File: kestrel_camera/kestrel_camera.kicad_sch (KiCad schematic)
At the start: 0 parts

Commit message: sensor pcb setup
creates kicad project for AISC110C sensor breakout board
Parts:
- added U1: (no value), AISC110C:AISC110C, symbol aisc110c:AISC110C
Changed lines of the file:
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@@
 	(generator_version "10.0")
 	(paper "A4")
+	(symbol
+		(lib_id "aisc110c:AISC110C")
+		(at 68.58 80.01 0)
+		(unit 1)
+		(body_style 1)
+		(exclude_from_sim no)
+		(in_bom yes)
+		(on_board yes)
+		(in_pos_files yes)
+		(dnp no)
+		(fields_autoplaced yes)
+		(property "Reference" "U1"
+			(at 83.4233 133.35 0)
+			(show_name no)
+			(do_not_autoplace no)
+			(effects
+				(font
+					(size 1.27 1.27)
+				)
+				(justify left)
+			)
+		)
+		(property "Value" ""
+			(at 68.58 80.01 0)
+			(show_name no)
+			(do_not_autoplace no)
+			(effects
+				(font
+					(size 1.27 1.27)
+				)
+			)
+		)
+		(property "Footprint" "AISC110C:AISC110C"
+			(at 68.58 80.01 0)
+			(hide yes)
+			(show_name no)
+			(do_not_autoplace no)
+			(effects
+				(font
+					(size 1.27 1.27)
+				)
+			)
+		)
+		(property "Datasheet" ""
+			(at 68.58 80.01 0)
+			(hide yes)
+			(show_name no)
+			(do_not_autoplace no)
+			(effects
+				(font
+					(size 1.27 1.27)
+				)
+			)
+		)
+		(property "Description" ""
+			(at 68.58 80.01 0)
+			(hide yes)
+			(show_name no)
+			(do_not_autoplace no)
+			(effects
+				(font
+					(size 1.27 1.27)
+				)
+			)
+		)
+		(pin "22"
+		)
+		(pin "9"
+		)
+		(pin "14"
+		)
+		(pin "26"
+		)
+		(pin "1"
+		)
+		(pin "28"
+		)
+		(pin "13"
+		)
+		(pin "18"
+		)
+		(pin "15"
+		)
+		(pin "21"
+		)
+		(pin "6"
+		)
+		(pin "17"
+		)
+		(pin "3"
+		)
+		(pin "4"
+		)
+		(pin "8"
+		)
+		(pin "20"
+		)
+		(pin "19"
+		)
+		(pin "12"
+		)
+		(pin "16"
+		)
+		(pin "10"
+		)
+		(pin "7"
+		)
+		(pin "11"
+		)
+		(pin "2"
+		)
+		(pin "5"
+		)
+		(pin "23"
+		)
+		(pin "24"
+		)
+		(pin "25"
+		)
+		(pin "27"
+		)
+		(pin "34"
+		)
+		(pin "47"
+		)
+		(pin "35"
+		)
+		(pin "51"
+		)
+		(pin "53"
+		)
+		(pin "55"
+		)
+		(pin "45"
+		)
+		(pin "49"
+		)
+		(pin "32"
+		)
+		(pin "46"
+		)
+		(pin "62"
+		)
+		(pin "40"
+		)
+		(pin "44"
+		)
+		(pin "39"
+		)
+		(pin "59"
+		)
+		(pin "36"
+		)
+		(pin "31"
+		)
+		(pin "29"
+		)
+		(pin "33"
+		)
+		(pin "38"
+		)
+		(pin "37"
+		)
+		(pin "42"
+		)
+		(pin "43"
+		)
+		(pin "30"
+		)
+		(pin "41"
+		)
+		(pin "48"
+		)
+		(pin "50"
+		)
+		(pin "52"
+		)
+		(pin "54"
+		)
+		(pin "56"
+		)
+		(pin "57"
+		)
+		(pin "58"
+		)
+		(pin "60"
+		)
+		(pin "61"
+		)
+		(pin "63"
+		)
+		(pin "64"
+		)
+		(instances
+			(project "kestrel_camera"
+				(path "/97a847c9-d989-41dc-b959-cfc0f8d7a8bf"
+					(reference "U1")
+					(unit 1)
+				)
+			)
+		)
+	)
 	(sheet_instances
 		(path "/"

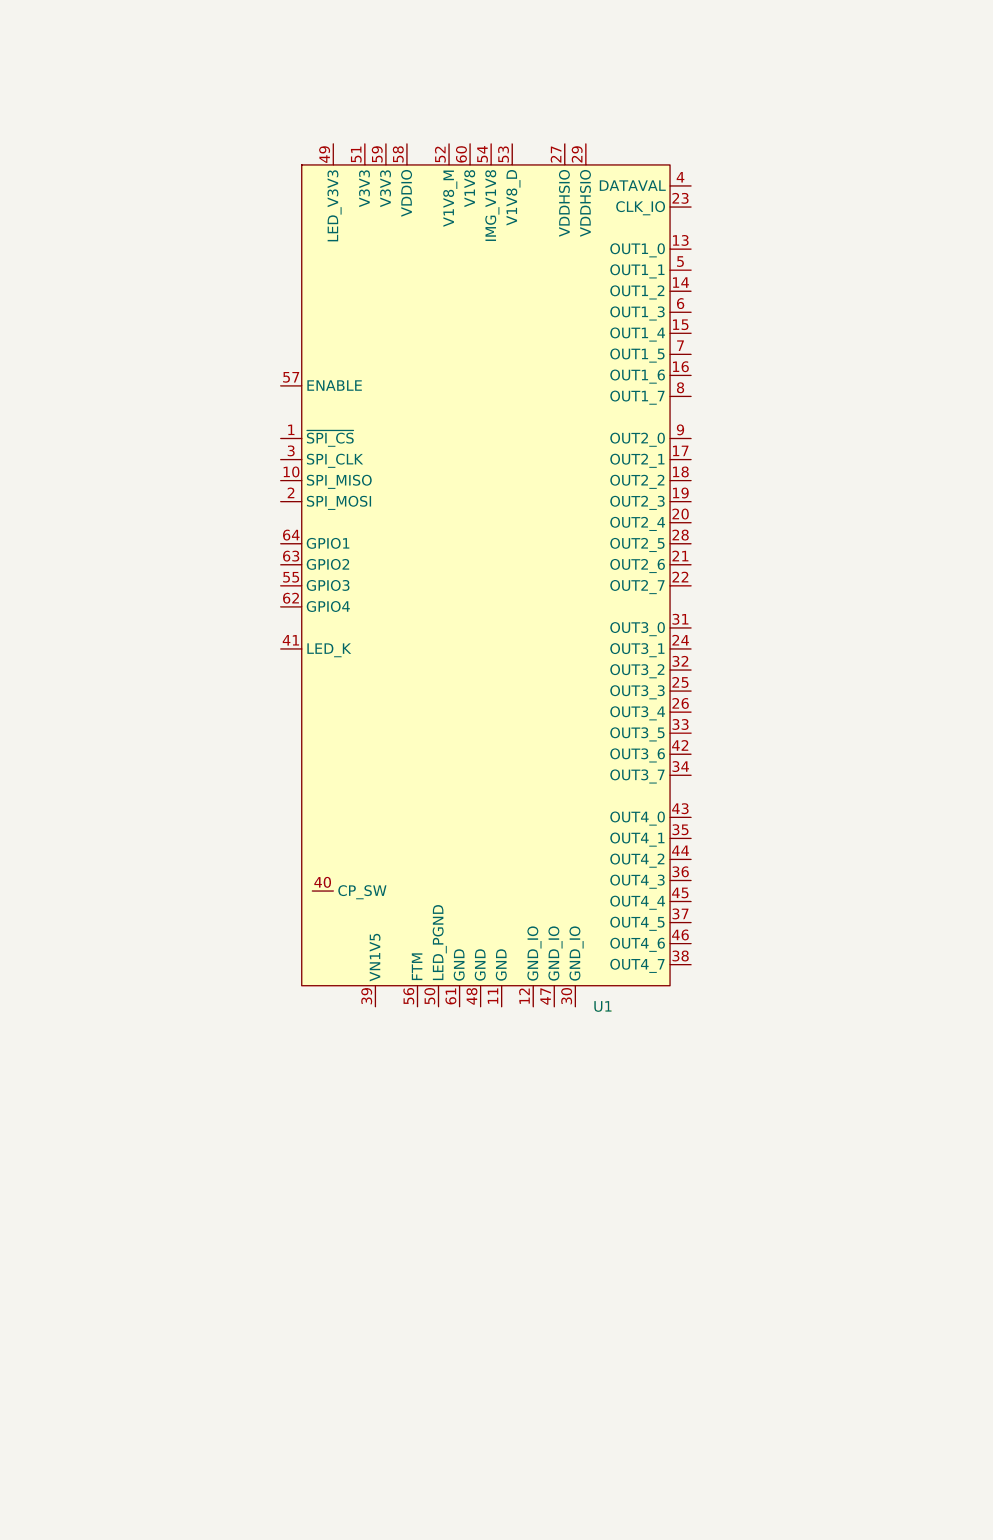
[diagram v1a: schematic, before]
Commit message: beginning setup for aisc110c sensor ic
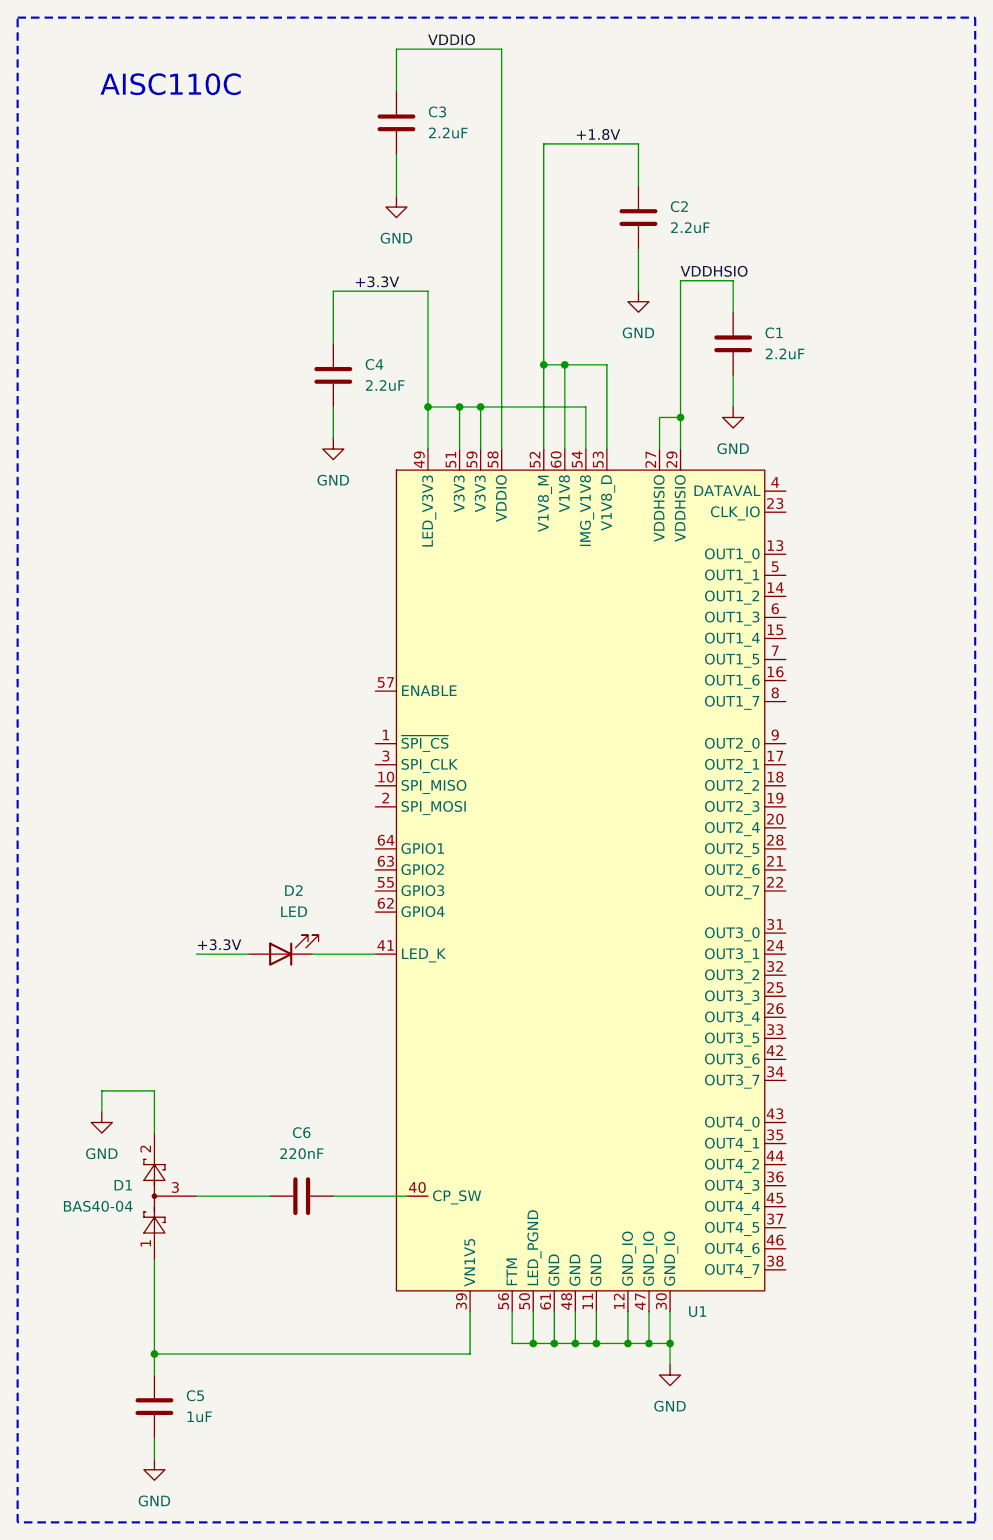
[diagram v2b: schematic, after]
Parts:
- added C1, C2, C3, C4: 2.2uF, symbol Device:C
- added C5: 1uF, symbol Device:C
- added C6: 220nF, symbol Device:C
- added D1: BAS40-04, Package_TO_SOT_SMD:SOT-23, symbol Diode:BAS40-04
- added D2: LED, symbol Device:LED
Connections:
- net GND: now reaches U1.11 (GND)
- net GND: now also U1.12 (GND_IO), U1.30 (GND_IO), U1.47 (GND_IO), U1.48 (GND), U1.50 (LED_PGND), U1.56 (FTM), U1.61 (GND), C1.2, C2.2, C3.2, C4.2, C5.2, D1.2
- net VDDHSIO: now reaches U1.27 (VDDHSIO)
- net VDDHSIO: now also U1.29 (VDDHSIO), C1.1
- net at U1.39 (VN1V5): now also C5.1, D1.1
- net at U1.40 (CP_SW): now also C6.2
- net at U1.41 (LED_K): now also D2.1 (K)
- net +3.3V: now reaches U1.49 (LED_V3V3)
- net +3.3V: now also U1.51 (V3V3), U1.54 (IMG_V1V8), U1.59 (V3V3), C4.1, D2.2 (A)
- net +1.8V: now reaches U1.52 (V1V8_M)
- net +1.8V: now also U1.53 (V1V8_D), U1.60 (V1V8), C2.1
- net VDDIO: now reaches U1.58 (VDDIO)
- net VDDIO: now also C3.1
- new net: C6.1, D1.3
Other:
- note added: "AISC110C"
- moved on the sheet: U1

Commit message: aisc110c fmc-hpc board schematic - revision 1
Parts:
- removed D1: BAS40-04, Package_TO_SOT_SMD:SOT-23, symbol Diode:BAS40-04
- added CR1: BAS40-04-E3-08, BAS40_04_E3_08:SOT_04-HE3-08_VIS, symbol BAS40_04_E3_08:BAS40-04-E3-08
- added J1: ASP-134602-01, ASP-134602-01:SAMTEC_ASP-134602-01, symbol ASP-134602-01:ASP-134602-01
- added J2: DEBUG_HEADER, Connector_PinHeader_2.54mm:PinHeader_2x08_P2.54mm_Vertical, symbol Connector_Generic_MountingPin:Conn_02x08_Odd_Even_MountingPin
- added R1: 10kR, Resistor_SMD:R_0603_1608Metric, symbol Device:R
- added TP1: V1V8_PWR, TestPoint:TestPoint_Pad_3.0x3.0mm, symbol Connector:TestPoint
- added TP10: D4_0, TestPoint:TestPoint_Pad_D1.5mm, symbol Connector:TestPoint
- added TP2: VDD_HSIO, TestPoint:TestPoint_Pad_3.0x3.0mm, symbol Connector:TestPoint
- added TP3: V3V3_PWR, TestPoint:TestPoint_Pad_3.0x3.0mm, symbol Connector:TestPoint
- added TP4: VN1V5_PWR, TestPoint:TestPoint_Pad_3.0x3.0mm, symbol Connector:TestPoint
- added TP5: CLK_IO, TestPoint:TestPoint_Pad_D1.5mm, symbol Connector:TestPoint
- added TP6: DATAVALID, TestPoint:TestPoint_Pad_D1.5mm, symbol Connector:TestPoint
- added TP7: D1_0, TestPoint:TestPoint_Pad_D1.5mm, symbol Connector:TestPoint
- added TP8: D2_0, TestPoint:TestPoint_Pad_D1.5mm, symbol Connector:TestPoint
- added TP9: D3_0, TestPoint:TestPoint_Pad_D1.5mm, symbol Connector:TestPoint
- C1, C2, C3, C4, C5, C6: footprint (none) -> Capacitor_SMD:C_0603_1608Metric
- D1: renamed from D2; footprint (none) -> LED_SMD:LED_0603_1608Metric
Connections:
- net VDDIO is gone; now on net V1V8: C3.1, U1.58 (VDDIO)
- net GND: now also CR1.1, J1.A1, J1.A12, J1.A13, J1.A16, J1.A17, J1.A20, J1.A21, J1.A24, J1.A25, J1.A28, J1.A29, J1.A32, J1.A33, J1.A36, J1.A37, J1.A4, J1.A40, J1.A5, J1.A8, J1.A9, J1.B10, J1.B11, J1.B14, J1.B15, J1.B18, J1.B19, J1.B2, J1.B22, J1.B23, J1.B26, J1.B27, J1.B3, J1.B30, J1.B31, J1.B34, J1.B35, J1.B38, J1.B39, J1.B6, J1.B7, J1.C1, J1.C12, J1.C13, J1.C16, J1.C17, J1.C20, J1.C21, J1.C24, J1.C25, J1.C28, J1.C29, J1.C32, J1.C33, J1.C36, J1.C38, J1.C4, J1.C40, J1.C5, J1.C8, J1.C9, J1.D10, J1.D13, J1.D16, J1.D19, J1.D2, J1.D22, J1.D25, J1.D28, J1.D3, J1.D37, J1.D39, J1.D6, J1.D7, J1.E1, J1.E11, J1.E14, J1.E17, J1.E20, J1.E23, J1.E26, J1.E29, J1.E32, J1.E35, J1.E38, J1.E4, J1.E40, J1.E5, J1.E8, J1.F12, J1.F15, J1.F18, J1.F2, J1.F21, J1.F24, J1.F27, J1.F3, J1.F30, J1.F33, J1.F36, J1.F39, J1.F6, J1.F9, J1.G1, J1.G11, J1.G14, J1.G17, J1.G20, J1.G23, J1.G26, J1.G29, J1.G32, J1.G35, J1.G38, J1.G4, J1.G40, J1.G5, J1.G8, J1.H12, J1.H15, J1.H18, J1.H21, J1.H24, J1.H27, J1.H3, J1.H30, J1.H33, J1.H36, J1.H39, J1.H6, J1.H9, J1.J1, J1.J11, J1.J14, J1.J17, J1.J20, J1.J23, J1.J26, J1.J29, J1.J32, J1.J35, J1.J38, J1.J4, J1.J40, J1.J5, J1.J8, J1.K12, J1.K15, J1.K18, J1.K2, J1.K21, J1.K24, J1.K27, J1.K3, J1.K30, J1.K33, J1.K36, J1.K39, J1.K40, J1.K6, J1.K9, J2.1 (Pin_1), J2.10 (Pin_10), J2.11 (Pin_11), J2.2 (Pin_2), J2.6 (Pin_6), J2.MP (MountPin), R1.2
- net VDDHSIO: now also TP2.1
- net SPI_CS: now reaches U1.1 (~{SPI_CS})
- net SPI_CS: now also J1.D8, J2.3 (Pin_3)
- net SPI_MISO: now reaches U1.10 (SPI_MISO)
- net SPI_MISO: now also J1.J24, J2.7 (Pin_7)
- net D1_0: now reaches U1.13 (OUT1_0)
- net D1_0: now also J1.C10, TP7.1
- net D1_2: now reaches U1.14 (OUT1_2)
- net D1_2: now also J1.D11
- net D1_4: now reaches U1.15 (OUT1_4)
- net D1_4: now also J1.H8
- net D1_6: now reaches U1.16 (OUT1_6)
- net D1_6: now also J1.H13
- net D2_1: now reaches U1.17 (OUT2_1)
- net D2_1: now also J1.H20
- net D2_2: now reaches U1.18 (OUT2_2)
- net D2_2: now also J1.G15
- net D2_3: now reaches U1.19 (OUT2_3)
- net D2_3: now also J1.C19
- net SPI_MOSI: now reaches U1.2 (SPI_MOSI)
- net SPI_MOSI: now also J1.F25, J2.9 (Pin_9)
- net D2_4: now reaches U1.20 (OUT2_4)
- net D2_4: now also J1.G18
- net D2_6: now reaches U1.21 (OUT2_6)
- net D2_6: now also J1.E25
- net D2_7: now reaches U1.22 (OUT2_7)
- net D2_7: now also J1.F23
- net CLK_IO: now reaches U1.23 (CLK_IO)
- net CLK_IO: now also J1.G6, TP5.1
- net D3_1: now reaches U1.24 (OUT3_1)
- net D3_1: now also J1.H22
- net D3_3: now reaches U1.25 (OUT3_3)
- net D3_3: now also J1.G28
- net D3_4: now reaches U1.26 (OUT3_4)
- net D3_4: now also J1.D23
- net D2_5: now reaches U1.28 (OUT2_5)
- net D2_5: now also J1.E21
- net SPI_CLK: now reaches U1.3 (SPI_CLK)
- net SPI_CLK: now also J1.D18, J2.5 (Pin_5)
- net D3_0: now reaches U1.31 (OUT3_0)
- net D3_0: now also J1.G36, TP9.1
- net D3_2: now reaches U1.32 (OUT3_2)
- net D3_2: now also J1.H35
- net D3_5: now reaches U1.33 (OUT3_5)
- net D3_5: now also J1.G30
- net D3_7: now reaches U1.34 (OUT3_7)
- net D3_7: now also J1.C26
- net D4_1: now reaches U1.35 (OUT4_1)
- net D4_1: now also J1.G24
- net D4_3: now reaches U1.36 (OUT4_3)
- net D4_3: now also J1.H28
- net D4_5: now reaches U1.37 (OUT4_5)
- net D4_5: now also J1.F28
- net D4_7: now reaches U1.38 (OUT4_7)
- net D4_7: now also J1.J31
- net at C5.1, U1.39 (VN1V5): now also CR1.2, TP4.1
- net DATAVAL: now reaches U1.4 (DATAVAL)
- net DATAVAL: now also J1.D14, TP6.1
- net D3_6: now reaches U1.42 (OUT3_6)
- net D3_6: now also J1.G21
- net D4_0: now reaches U1.43 (OUT4_0)
- net D4_0: now also J1.D20, TP10.1
- net D4_2: now reaches U1.44 (OUT4_2)
- net D4_2: now also J1.G33
- net D4_4: now reaches U1.45 (OUT4_4)
- net D4_4: now also J1.H32
- net D4_6: now reaches U1.46 (OUT4_6)
- net D4_6: now also J1.J28
- net D1_1: now reaches U1.5 (OUT1_1)
- net D1_1: now also J1.H10
- net GPIO3: now reaches U1.55 (GPIO3)
- net GPIO3: now also J1.K28, J2.15 (Pin_15)
- net ENABLE: now reaches U1.57 (ENABLE)
- net ENABLE: now also J1.C15, J2.12 (Pin_12), R1.1
- net D1_3: now reaches U1.6 (OUT1_3)
- net D1_3: now also J1.G13
- net GPIO4: now reaches U1.62 (GPIO4)
- net GPIO4: now also J1.C22, J2.16 (Pin_16)
- net GPIO2: now reaches U1.63 (GPIO2)
- net GPIO2: now also J1.D26, J2.14 (Pin_14)
- net GPIO1: now reaches U1.64 (GPIO1)
- net GPIO1: now also J1.H37, J2.13 (Pin_13)
- net D1_5: now reaches U1.7 (OUT1_5)
- net D1_5: now also J1.G9
- net D1_7: now reaches U1.8 (OUT1_7)
- net D1_7: now also J1.H16
- net D2_0: now reaches U1.9 (OUT2_0)
- net D2_0: now also J1.K25, TP8.1
- net at C6.1: now also CR1.3
- net +1.8V renamed V1V8
- net V1V8: now also U1.54 (IMG_V1V8), J2.8 (Pin_8), TP1.1; no longer U1.52 (V1V8_M)
- net +3.3V renamed V3V3
- net V3V3: now also U1.52 (V1V8_M), J1.D40, J2.4 (Pin_4), TP3.1; no longer U1.54 (IMG_V1V8)
- no-connect marks 0 -> 196
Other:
- note added: "DEBUG"
- note added: "FMC-HPC Connector"
- title: (none) -> AISC110C FMC-HPC Board
- moved on the sheet: C1, C2, C3, C4, C5, C6, D1, U1
